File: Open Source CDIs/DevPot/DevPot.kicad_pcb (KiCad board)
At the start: 2 copper layers, 45 x 31 mm, 21 parts, among them J1 MAG, J2 lD, J3 GtD, J4 scrD, J5 AtG, J6 COIL, J7 aD, J8 aC, Q1 TIC106

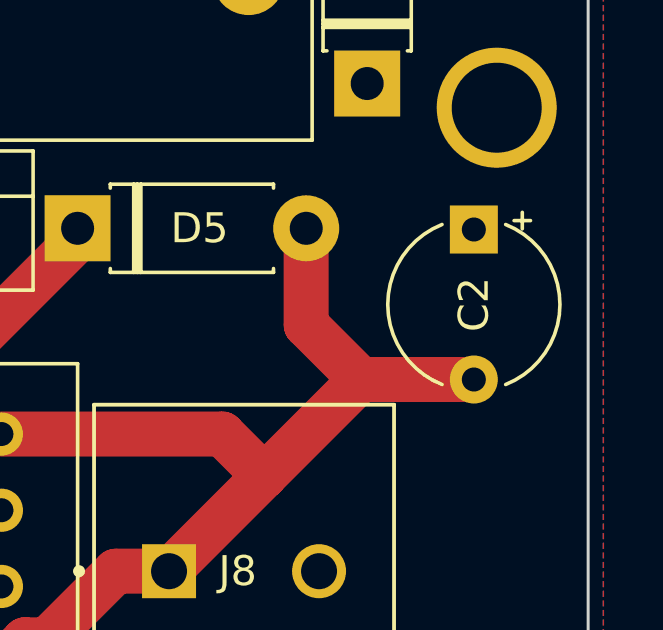
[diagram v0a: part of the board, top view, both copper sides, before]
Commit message: Added new CDIs and updated README
Added the DevPot_v2 CDI, updated the readme to include all of the new CDIs and included images for each. Also add production exports for all the boards.
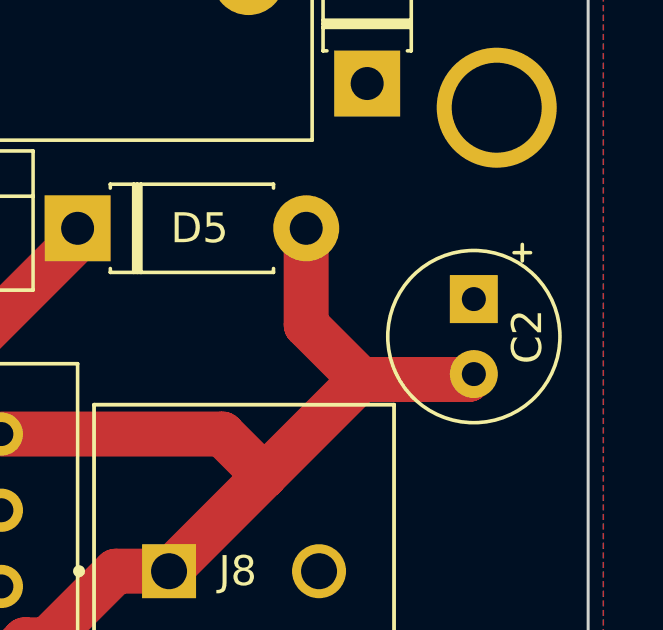
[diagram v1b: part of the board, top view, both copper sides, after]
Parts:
- C2: footprint Capacitor_THT:CP_Radial_Tantal_D5.5mm_P5.00mm -> Capacitor_THT:CP_Radial_Tantal_D5.5mm_P2.50mm
- moved C2 2.32 mm to (165.4, 79.8)
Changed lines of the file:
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@@
     (pad "2" thru_hole circle (at 2.5 0) (size 1.8 1.8) (drill 1.2) (layers "*.Cu" "*.Mask")
       (net 3 "GND") (pinfunction "Pin_2") (pintype "passive") (solder_mask_margin 0.102))
+    (model "${KIPRJMOD}/1792863.step"
+      (offset (xyz -5 -3 0))
+      (scale (xyz 1 1 1))
+      (rotate (xyz 0 0 0))
+    )
   )
   (footprint "Diode_THT:D_DO-41_SOD81_P7.62mm_Horizontal" (layer "F.Cu")
@@
       (net 7 "Net-(D5-K)") (pinfunction "Pin_2") (pintype "passive"))
   )
-  (footprint "Capacitor_THT:CP_Radial_Tantal_D5.5mm_P5.00mm" (layer "F.Cu")
-    (at 165.354 77.51 -90)
-    (descr "CP, Radial_Tantal series, Radial, pin pitch=5.00mm, , diameter=5.5mm, Tantal Electrolytic Capacitor, http://cdn-reichelt.de/documents/datenblatt/B300/TANTAL-TB-Serie%23.pdf")
-    (tags "CP Radial_Tantal series Radial pin pitch 5.00mm  diameter 5.5mm Tantal Electrolytic Capacitor")
+  (footprint "Capacitor_THT:CP_Radial_Tantal_D5.5mm_P2.50mm" (layer "F.Cu")
+    (at 165.354 79.829631 -90)
+    (descr "CP, Radial_Tantal series, Radial, pin pitch=2.50mm, , diameter=5.5mm, Tantal Electrolytic Capacitor, http://cdn-reichelt.de/documents/datenblatt/B300/TANTAL-TB-Serie%23.pdf")
+    (tags "CP Radial_Tantal series Radial pin pitch 2.50mm  diameter 5.5mm Tantal Electrolytic Capacitor")
     (property "Sheetfile" "DevPot.kicad_sch")
     (property "Sheetname" "")
@@
     (property "ki_keywords" "cap capacitor")
     (attr through_hole)
-    (fp_text reference "C2" (at 2.5 0 90) (layer "F.SilkS")
-        (effects (font (size 1 1) (thickness 0.15)))
-    )
-    (fp_text value "0.47u" (at 2.5 4 90) (layer "F.Fab")
-        (effects (font (size 1 1) (thickness 0.15)))
-    )
-    (fp_text user "${REFERENCE}" (at 2.5 0 90) (layer "F.Fab")
-        (effects (font (size 1 1) (thickness 0.15)))
-    )
-    (fp_line (start -0.572262 -1.615) (end -0.022262 -1.615)
-      (stroke (width 0.12) (type solid)) (layer "F.SilkS"))
-    (fp_line (start -0.297262 -1.89) (end -0.297262 -1.34)
-      (stroke (width 0.12) (type solid)) (layer "F.SilkS"))
-    (fp_arc (start -0.167077 -1.06) (mid 2.5 -2.87) (end 5.167077 -1.06)
-      (stroke (width 0.12) (type solid)) (layer "F.SilkS"))
-    (fp_arc (start 5.167077 1.06) (mid 2.5 2.87) (end -0.167077 1.06)
-      (stroke (width 0.12) (type solid)) (layer "F.SilkS"))
-    (fp_circle (center 2.5 0) (end 6.22 0)
+    (fp_text reference "C2" (at 1.25 -1.778 -90) (layer "F.SilkS")
+        (effects (font (size 1 1) (thickness 0.15)))
+    )
+    (fp_text value "0.47u" (at 1.25 4 -90) (layer "F.Fab")
+        (effects (font (size 1 1) (thickness 0.15)))
+    )
+    (fp_text user "${REFERENCE}" (at 1.25 0 -90) (layer "F.Fab")
+        (effects (font (size 1 1) (thickness 0.15)))
+    )
+    (fp_line (start -1.822262 -1.615) (end -1.272262 -1.615)
+      (stroke (width 0.12) (type solid)) (layer "F.SilkS"))
+    (fp_line (start -1.547262 -1.89) (end -1.547262 -1.34)
+      (stroke (width 0.12) (type solid)) (layer "F.SilkS"))
+    (fp_circle (center 1.25 0) (end 4.12 0)
+      (stroke (width 0.12) (type solid)) (fill none) (layer "F.SilkS"))
+    (fp_circle (center 1.25 0) (end 4.25 0)
       (stroke (width 0.05) (type solid)) (fill none) (layer "F.CrtYd"))
-    (fp_line (start 0.150869 -1.1975) (end 0.700869 -1.1975)
-      (stroke (width 0.1) (type solid)) (layer "F.Fab"))
-    (fp_line (start 0.425869 -1.4725) (end 0.425869 -0.9225)
-      (stroke (width 0.1) (type solid)) (layer "F.Fab"))
-    (fp_circle (center 2.5 0) (end 5.25 0)
+    (fp_line (start -1.099131 -1.1975) (end -0.549131 -1.1975)
+      (stroke (width 0.1) (type solid)) (layer "F.Fab"))
+    (fp_line (start -0.824131 -1.4725) (end -0.824131 -0.9225)
+      (stroke (width 0.1) (type solid)) (layer "F.Fab"))
+    (fp_circle (center 1.25 0) (end 4 0)
       (stroke (width 0.1) (type solid)) (fill none) (layer "F.Fab"))
     (pad "1" thru_hole rect (at 0 0 270) (size 1.6 1.6) (drill 0.8) (layers "*.Cu" "*.Mask")
       (net 3 "GND") (pintype "passive"))
-    (pad "2" thru_hole circle (at 5 0 270) (size 1.6 1.6) (drill 0.8) (layers "*.Cu" "*.Mask")
+    (pad "2" thru_hole circle (at 2.5 0 270) (size 1.6 1.6) (drill 0.8) (layers "*.Cu" "*.Mask")
       (net 4 "Net-(D5-A)") (pintype "passive"))
-    (model "${KICAD6_3DMODEL_DIR}/Capacitor_THT.3dshapes/CP_Radial_Tantal_D5.5mm_P5.00mm.wrl"
+    (model "${KICAD6_3DMODEL_DIR}/Capacitor_THT.3dshapes/CP_Radial_Tantal_D5.5mm_P2.50mm.wrl"
       (offset (xyz 0 0 0))
       (scale (xyz 1 1 1))
@@
   (segment (start 150.388 91.186) (end 151.13 91.186) (width 1.5) (layer "F.Cu") (net 4))
   (segment (start 156.972 84.328) (end 158.369 85.725) (width 1.5) (layer "F.Cu") (net 4))
-  (segment (start 165.354 82.51) (end 161.584 82.51) (width 1.5) (layer "F.Cu") (net 4))
   (segment (start 158.369 85.725) (end 155.194 88.9) (width 1.5) (layer "F.Cu") (net 4))
   (segment (start 161.584 82.51) (end 158.369 85.725) (width 1.5) (layer "F.Cu") (net 4))
   (segment (start 151.13 91.186) (end 153.416 88.9) (width 1.5) (layer "F.Cu") (net 4))
+  (segment (start 165.354 82.329631) (end 165.173631 82.51) (width 1.5) (layer "F.Cu") (net 4))
   (segment (start 149.606 84.328) (end 156.972 84.328) (width 1.5) (layer "F.Cu") (net 4))
   (segment (start 159.766 80.692) (end 161.584 82.51) (width 1.5) (layer "F.Cu") (net 4))
   (segment (start 148.356 93.218) (end 150.388 91.186) (width 1.5) (layer "F.Cu") (net 4))
+  (segment (start 165.173631 82.51) (end 161.584 82.51) (width 1.5) (layer "F.Cu") (net 4))
   (segment (start 153.416 88.9) (end 155.194 88.9) (width 1.5) (layer "F.Cu") (net 4))
   (segment (start 131.318 70.568) (end 127 66.25) (width 1.5) (layer "F.Cu") (net 5))
